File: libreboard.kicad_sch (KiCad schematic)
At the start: 41 parts, among them J100 Screw Terminal, J101 Screw Terminal, J11 USB_C_Receptacle_USB2.0, J51 12V Fan 1, J52 12V Fan 2, J53 12V Fan 3, J54 12V Fan 4, Q1 CSD18511Q5A, U4 LM5155DSSR

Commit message: starting to trace
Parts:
- added C31: 0.1uF, Capacitor_SMD:C_0402_1005Metric, symbol Device:C_Small
- added C51: 4.7 uF, Capacitor_SMD:C_0805_2012Metric, symbol Device:C_Small
- added C52, C53: 100 nF, Capacitor_SMD:C_0805_2012Metric, symbol Device:C_Small
- added C54, C55: 47 uF, Capacitor_SMD:C_0805_2012Metric, symbol Device:C_Small
- added L3: 5.6 uH, Inductor_SMD:L_Coilcraft_XAL6060-XXX, symbol Device:L
- added R21, R22, R23, R24, R29, R30: 10k, Resistor_SMD:R_0402_1005Metric, symbol Device:R_Small
- added R31: 22k, Resistor_SMD:R_0402_1005Metric, symbol Device:R_Small
- added R32: 33k, Resistor_SMD:R_0402_1005Metric, symbol Device:R_Small
- added R42: 30.9 kΩ, Resistor_SMD:R_0603_1608Metric, symbol Device:R_Small
- added R43, R44: 100 kΩ, Resistor_SMD:R_0603_1608Metric, symbol Device:R_Small
- added R45: 19.1 kΩ, Resistor_SMD:R_0603_1608Metric, symbol Device:R_Small
- added U10: EMC2305-x-AP, Package_DFN_QFN:Texas_RGV0016A_VQFN-16-1EP_4x4mm_P0.65mm_EP2.1x2.1mm_ThermalVias, symbol Driver_Motor:EMC2305-x-AP
- added U14: LMR51450FNDRRR, libreboard:CONV_LMR51450FNDRRR, symbol LMR51450FNDRRR:LMR51450FNDRRR
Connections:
- net +12V: now also J51.2 (12V), J52.2, J53.2, J54.2
- net +3.3v: now also C31.1, R21.1, R22.1, R23.1, R24.1, R29.2, R30.2, R31.2, R32.2, U10.3 (VDD)
- net +VDC: now also C51.1, C52.1, U14.10 (VIN), U14.11 (VIN__1), U14.12 (VIN__2), U14.9 (EN)
- net CM5_GPIO ( Ethernet, GPIO, SDCARD)/ID_SC: now also R30.1, U10.2 (SMCLK)
- net CM5_GPIO ( Ethernet, GPIO, SDCARD)/ID_SD: now also R29.1, U10.1 (SMDATA)
- net GND: now also J51.1 (GND), J52.1, J53.1, J54.1, C31.2, C51.2, C52.2, C54.2, C55.2, R42.2, R45.2, U10.17 (GND), U14.13 (PGND), U14.8 (AGND)
- net at J51.3 (TACH): now also R24.2, U10.6 (TACH1)
- net at J51.4 (PWM): now also U10.5 (PWM1)
- net at J52.3: now also R23.2, U10.8 (TACH2)
- net at J52.4: now also U10.7 (PWM2)
- net at J54.3: now also R21.2, U10.14 (TACH4)
- net at J54.4: now also U10.13 (PWM4)
- net at J53.3: now also R22.2, U10.10 (TACH3)
- net at J53.4: now also U10.9 (PWM3)
- new net: R44.2, R45.1, U14.7 (FB)
- new net: C53.2, L3.1, U14.1 (SW), U14.2 (SW__1), U14.3 (SW__2)
- new net: C53.1, U14.4 (BOOT)
- new net: R43.1, U14.5 (PG)
- new net: R42.1, U14.6 (RT)
- new net: R31.1, U10.11 (CLK)
- new net: R32.1, U10.4 (ADDR_SEL)
- new net +5V: C54.1, C55.1, L3.2, R43.2, R44.1
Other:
- sheet CM5_HighSpeed ports: added none; removed ID_SC, ID_SD
- note added: "https://webench.ti.com/appinfo/webench/scripts/SDP.cgi?ID=394641B4FF50B9DB"
- moved on the sheet: H1, H2, H3, H4, H5, H6, H7, H8, J100, J101, J51, J52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

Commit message: voltage regulator refactoring
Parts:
- removed C20, C21: 10uF, Capacitor_SMD:C_1210_3225Metric, symbol Device:C
- removed C22: 10nF, Capacitor_SMD:C_0603_1608Metric, symbol Device:C
- removed C23: 1uF, Capacitor_SMD:C_0603_1608Metric, symbol Device:C
- removed C24: 10pF, Capacitor_SMD:C_0201_0603Metric, symbol Device:C
- removed C25: 220nF, Capacitor_SMD:C_1812_4532Metric, symbol Device:C
- removed C26: 330pF, Capacitor_SMD:C_0402_1005Metric, symbol Device:C
- removed C27: 560pF, Capacitor_SMD:C_0805_2012Metric, symbol Device:C
- removed C28: 1uF, Capacitor_SMD:C_1206_3216Metric, symbol Device:C
- removed C29: 22uF, Capacitor_SMD:C_1210_3225Metric, symbol Device:C
- removed C30: 100pF, Capacitor_SMD:C_0805_2012Metric, symbol Device:C
- removed C51: 4.7 uF, Capacitor_SMD:C_0805_2012Metric, symbol Device:C_Small
- removed D4: 455mV 20A, Package_TO_SOT_THT:TO-220-2_Horizontal_TabDown, symbol Device:D_Schottky
- removed L2: 2.2uH, Inductor_SMD:L_Bourns_SRF1260, symbol Device:L_Iron_Coupled
- removed Q1: CSD18511Q5A, Package_SON:VSONP-8-1EP_5x6_P1.27mm, symbol emberone:CSD18511Q5A
- removed R11: 68.1kΩ, Resistor_SMD:R_0603_1608Metric, symbol Device:R
- removed R13: 100Ω, Resistor_SMD:R_0603_1608Metric, symbol Device:R
- removed R18: 51.1kΩ, Resistor_SMD:R_0603_1608Metric, symbol Device:R
- removed R19: 4.7kΩ, Resistor_SMD:R_0603_1608Metric, symbol Device:R
- removed R20: 18mΩ, Resistor_SMD:R_0612_1632Metric, symbol Device:R
- removed R42: 30.9 kΩ, Resistor_SMD:R_0603_1608Metric, symbol Device:R_Small
- removed R43, R44: 100 kΩ, Resistor_SMD:R_0603_1608Metric, symbol Device:R_Small
- removed R45: 19.1 kΩ, Resistor_SMD:R_0603_1608Metric, symbol Device:R_Small
- removed R6: 43.2kΩ, Resistor_SMD:R_0603_1608Metric, symbol Device:R
- removed R7: 6.49kΩ, Resistor_SMD:R_0603_1608Metric, symbol Device:R
- removed R8: 9.31kΩ, Resistor_SMD:R_0603_1608Metric, symbol Device:R
- removed U14: LMR51450FNDRRR, libreboard:CONV_LMR51450FNDRRR, symbol LMR51450FNDRRR:LMR51450FNDRRR
- removed U4: LM5155DSSR, libreboard:DSS0012B, symbol 2025-05-04_16-39-33:LM5155DSSR
- added C20: 39µF, Capacitor_SMD:CP_Elec_8x6.7, symbol Device:C_Polarized_Small
- added C21: 10µF, Capacitor_SMD:C_0402_1005Metric, symbol Device:C_Small
- added C22: 1µF, Capacitor_SMD:C_0603_1608Metric, symbol Device:C_Small
- added C23: 4.7µF, Capacitor_SMD:C_0603_1608Metric, symbol Device:C_Small
- added C24, C25, C65: 100nF, Capacitor_SMD:C_0603_1608Metric, symbol Device:C_Small
- added C26: 56µF, Capacitor_SMD:CP_Elec_5x5.9, symbol Device:C_Polarized_Small
- added C27, C28, C29: 33µF, Capacitor_SMD:C_0603_1608Metric, symbol Device:C_Small
- added C30, C64: 1µF, Capacitor_SMD:C_0402_1005Metric, symbol Device:C_Small
- added C51: 22µF, Capacitor_SMD:CP_Elec_6.3x5.9, symbol Device:C_Polarized_Small
- added C60: 3.9pF, Capacitor_SMD:C_0603_1608Metric, symbol Device:C_Small
- added C61: 470pF, Capacitor_SMD:C_0603_1608Metric, symbol Device:C_Small
- added C62: 560pF, Capacitor_SMD:C_0603_1608Metric, symbol Device:C_Small
- added C63: 1pF, Capacitor_SMD:C_0603_1608Metric, symbol Device:C_Small
- added C66, C67, C68: 47µF, Capacitor_SMD:C_0603_1608Metric, symbol Device:C_Small
- added C69: 270µF, Capacitor_SMD:CP_Elec_6.3x9.9, symbol Device:C_Polarized_Small
- added L2: 4.7µH, Inductor_SMD:L_Bourns_SRN8040TA, symbol Device:L
- added R11, R20: 105kΩ, Resistor_SMD:R_0603_1608Metric, symbol Device:R_Small
- added R13: 50kΩ, Resistor_SMD:R_0603_1608Metric, symbol Device:R_Small
- added R18, R6: 887kΩ, Resistor_SMD:R_0603_1608Metric, symbol Device:R_Small
- added R19, R7: 100kΩ, Resistor_SMD:R_0603_1608Metric, symbol Device:R_Small
- added R8: 48.7kΩ, Resistor_SMD:R_0603_1608Metric, symbol Device:R_Small
- added U14, U4: PTPS55289RYQR, libreboard:RYQ0021A-MFG, symbol TPS55289:PTPS55289RYQR
- C18, C9: value 100n -> 100nF; Dist. P/N (none) -> 478-11504-2-ND; Distributor (none) -> Digikey; Field4 Farnell -> (none); Field5 2611911 -> (none); Field6 RM EMK105 B7104KV-F -> (none); Field7 TAIYO YUDEN EUROPE GMBH -> (none); Field8 110091611 -> (none); Manf. P/N (none) -> 04026D104KAT4A; Manufacturer (none) -> Kyocera; Part Description 0.1uF 10% 16V Ceramic Capacitor X7R 0402 (1005 Metric) -> Capacitor, Ceramic, 0.1µF, ±10%, 6.3V, X5R, 0402 (1005m)
- C31: value 0.1uF -> 0.1µF; Dist. P/N (none) -> 478-11504-2-ND; Distributor (none) -> Digikey; Manf. P/N (none) -> 04026D104KAT4A; Manufacturer (none) -> Kyocera; Part Description (none) -> Capacitor, Ceramic, 0.1µF, ±10%, 6.3V, X5R, 0402 (1005m)
- C52: value 100 nF -> 10µF; footprint Capacitor_SMD:C_0805_2012Metric -> Capacitor_SMD:C_0402_1005Metric; Distributor (none) -> Digikey
- C53: value 100 nF -> 4.7µF; footprint Capacitor_SMD:C_0805_2012Metric -> Capacitor_SMD:C_0603_1608Metric; Distributor (none) -> Digikey
- C54: value 47 uF -> 1µF; footprint Capacitor_SMD:C_0805_2012Metric -> Capacitor_SMD:C_0603_1608Metric; Distributor (none) -> Digikey
- C55: value 47 uF -> 100nF; footprint Capacitor_SMD:C_0805_2012Metric -> Capacitor_SMD:C_0603_1608Metric; Distributor (none) -> Digikey
- H1, H2, H3, H4, H5, H6, H7, H8: Dist. P/N (none) -> nf; Distributor (none) -> nf; Field4 nf -> (none); Field5 nf -> (none); Field6 nf -> (none); Field7 nf -> (none)
- J100, J101: Dist. P/N (none) -> 36-7771-ND; Distributor (none) -> Digikey; Manf. P/N (none) -> 7771; Manufacturer (none) -> Keystone; Part Description (none) -> Screw Terminal, M3
- J11: footprint Connector_USB:USB_C_Receptacle_GCT_USB4105-xx-A_16P_TopMnt_Horizontal -> Connector_USB:USB_C_Receptacle_GCT_USB4105-GF-A_16P_TopMnt_Horizontal; Dist. P/N (none) -> 2073-USB4105-GF-ATR-ND; Distributor (none) -> Digikey; Field5 USBF31-0171 -> (none); Field6 USBF31-0171 -> (none); Field7 MTCONN -> (none); Manf. P/N (none) -> USB4105-GF-A; Manufacturer (none) -> GCT; Part Description USBC USB2 data and power connector -> Connector, USB-C, 2.0 data and power
- J51: Dist. P/N (none) -> WM4330-ND; Distributor (none) -> Digikey; Manf. P/N (none) -> 0470531000; Manufacturer (none) -> Molex; Part Description (none) -> Connector, Fan 1, 12V, 4 pin
- J52: Dist. P/N (none) -> WM4330-ND; Distributor (none) -> Digikey; Manf. P/N (none) -> 0470531000; Manufacturer (none) -> Molex; Part Description (none) -> Connector, Fan 2, 12V, 4 pin
- J53: Dist. P/N (none) -> WM4330-ND; Distributor (none) -> Digikey; Manf. P/N (none) -> 0470531000; Manufacturer (none) -> Molex; Part Description (none) -> Connector, Fan 3, 12V, 4 pin
- J54: Dist. P/N (none) -> WM4330-ND; Distributor (none) -> Digikey; Manf. P/N (none) -> 0470531000; Manufacturer (none) -> Molex; Part Description (none) -> Connector, Fan 4, 12V, 4 pin
- L3: value 5.6 uH -> 4.7µH; footprint Inductor_SMD:L_Coilcraft_XAL6060-XXX -> Inductor_SMD:L_Bourns_SRN8040TA; Dist. P/N (none) -> SRN8040-4R7YCT-ND; Distributor (none) -> Digikey; Manf. P/N (none) -> SRN8040-4R7Y; Manufacturer (none) -> Coilcraft; Part Description (none) -> FIXED IND 4.7UH 4.1A 24 MOHM SMD
- R21, R22, R23, R24, R29, R30: value 10k -> 10kΩ; Dist. P/N (none) -> 10-ERJ-U02F1002XTR-ND; Distributor (none) -> Digikey; Manf. P/N (none) -> ERJ-U02F1002X; Manufacturer (none) -> Panasonic; Part Description (none) -> Resistor, 10kΩ, ±1%, 0.1W, SMD 0402 (1005m)
- R31: value 22k -> 22kΩ; Dist. P/N (none) -> P22.0KLTR-ND; Distributor (none) -> Digikey; Manf. P/N (none) -> ERJ-2RKF2202X; Manufacturer (none) -> Panasonic; Part Description (none) -> Resistor, 22kΩ, ±1%, 0.1W, SMD 0402 (1005m)
- R32: value 33k -> 33kΩ; Dist. P/N (none) -> 10-ERJ-U02F3302XTR-ND; Distributor (none) -> Digikey; Manf. P/N (none) -> ERJ-U02F3302X; Manufacturer (none) -> Panasonic; Part Description (none) -> Resistor, 33kΩ, ±1%, 0.1W, SMD 0402 (1005m)
- R9: value 2.2K 1% -> 2.2kΩ; Dist. P/N (none) -> P2.20KLTR-ND; Distributor (none) -> Digikey; Field4 Farnell -> (none); Manf. P/N (none) -> ERJ-2RKF2201X; Manufacturer (none) -> Panasonic; Part Description Resistor 2.2K M1005 1% 63mW -> Resistor, 2.2kΩ, ±1%, 0.1W, SMD 0402 (1005m)
- U10: Dist. P/N (none) -> EMC2305-1-AP-TR-ND; Distributor (none) -> Digikey; Manf. P/N (none) -> EMC2305-1-AP-TR; Manufacturer (none) -> Microchip Technology; Part Description (none) -> Motor Driver, PWM, 16-QFN, 4x4
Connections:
- net +12V: now also C26.1, C27.1, C28.1, C29.1, C30.1, U4.11 (VOUT), U4.12 (ISP), U4.13 (ISN)
- net +5v: now also C64.1, C66.1, C67.1, C68.1, C69.1, U14.11 (VOUT), U14.12 (ISP), U14.13 (ISN)
- net +VDC: now also C54.1, C20.1, C21.1, C22.1, C51.1, R18.1, R6.1, U14.7 (VIN), U4.7 (VIN)
- net GND: now also C53.2, C20.2, C21.2, C22.2, C23.2, C26.2, C27.2, C28.2, C29.2, C30.2, C51.2, C60.2, C63.2, C64.2, C66.2, C67.2, C68.2, C69.2, R11.2, R13.2, R19.2, R20.2, R7.2, R8.2, U14.17 (AGND), U14.2 (MODE), U14.5 (DITH_SYNC), U14.9 (PGND), U4.17 (AGND), U4.2 (MODE), U4.5 (DITH_SYNC), U4.9 (PGND); no longer C55.2
- net at L3.1: now also C55.1, U14.8 (SW1); no longer C53.2
- net at C53.1: now also U14.18 (VCC), U14.21 (EXTVCC)
- removed net +5V: C54.1, C55.1, L3.2
- new net: C62.1, C63.1, U14.15 (COMP)
- new net: R6.2, R7.1, U4.1 (EN_UVLO)
- new net: C25.1, L2.2, U4.10 (SW2)
- new net: C60.1, C61.1, U4.15 (COMP)
- new net: C23.1, U4.18 (VCC), U4.21 (EXTVCC)
- new net: C25.2, U4.19 (BOOT2)
- new net: C24.2, U4.20 (BOOT1)
- new net: R8.1, U4.6 (FSW)
- new net: C24.1, L2.1, U4.8 (SW1)
- new net: C62.2, R20.1
- new net: C65.1, L3.2, U14.10 (SW2)
- new net: C61.2, R11.1
- new net: R13.1, U14.6 (FSW)
- new net: C55.2, U14.20 (BOOT1)
- new net: R18.2, R19.1, U14.1 (EN_UVLO)
- new net: C65.2, U14.19 (BOOT2)
- no-connect marks 2 -> 6
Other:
- note added: "https://webench.ti.com/appinfo/webench/scripts/SDP.cgi?ID=1FB30C76529277AD"
- note added: "https://webench.ti.com/appinfo/webench/scripts/SDP.cgi?ID=DFB867964FE642FB"
- note removed: "https://webench.ti.com/appinfo/webench/scripts/SDP.cgi?ID=394641B4FF50B9DB"

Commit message: place all components
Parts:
- C22, C23, C24, C25, C27, C28, C29, C53, C54, C55, C60, C61, C62, C63, C65, C66, C67, C68: footprint Capacitor_SMD:C_0603_1608Metric -> Capacitor_SMD:C_0402_1005Metric
- J100, J101: footprint libreboard:7770-screw-terminal -> libreboard:KEYSTONE_7790; Dist. P/N 36-7771-ND -> 36-7790-ND; Manf. P/N 7771 -> 7790
- J54: now not fitted
- R11, R13, R18, R19, R20, R6, R7, R8: footprint Resistor_SMD:R_0603_1608Metric -> Resistor_SMD:R_0402_1005Metric

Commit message: updates BOM, sychronizes PCB from schematic, & includes error report.
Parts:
- C20: Dist. P/N (none) -> 399-A770KE396M1HLAS042TR-ND; Distributor (none) -> Digikey; Manf. P/N (none) -> A770KE396M1HLAS042; Manufacturer (none) -> Kemet; Part Description (none) -> Capacitor, Aluminum, 39µF, ±20%, 50V, 42mΩ ESR
- C21, C52: Dist. P/N (none) -> 478-KGM05CR50J106MHTR-ND; Manf. P/N (none) -> 04026D106MAT2A; Manufacturer (none) -> Kyocera; Part Description (none) -> Capacitor, Ceramic, 10µF, ±20%, 6.3V, X5R, 0402 (1005m)
- C22, C30, C54, C64: Dist. P/N (none) -> 478-KGM05AR50J105KHTR-ND; Manf. P/N (none) -> 04026D105KAT2A; Manufacturer (none) -> Kyocera; Part Description (none) -> Capacitor, Ceramic, 1µF, ±10%, 6.3V, X5R, 0402 (1005m)
- C23, C53: footprint Capacitor_SMD:C_0402_1005Metric -> Capacitor_SMD:C_1206_3216Metric; Dist. P/N (none) -> 478-KGM31AR71H475KUTR-ND; Manf. P/N (none) -> 12065C475KAT2A; Manufacturer (none) -> Kyocera; Part Description (none) -> Capacitor, Ceramic, 4.7µF, ±10%, 50V, X7R, 1206 (3216m)
- C24, C25, C55, C65: Dist. P/N (none) -> 478-11504-2-ND; Manf. P/N (none) -> 04026D104KAT4A; Manufacturer (none) -> Kyocera; Part Description (none) -> Capacitor, Ceramic, 0.1µF, ±10%, 6.3V, X5R, 0402 (1005m)
- C26: Dist. P/N (none) -> P122099TR-ND; Distributor (none) -> Digikey; Manf. P/N (none) -> 20SVF56M; Manufacturer (none) -> Panasonic; Part Description (none) -> Capacitor, Aluminum, 56µF, ±20%, 20V, 30mΩ ESR
- C51: Dist. P/N (none) -> 399-A768EB226M1HLAE048TR-ND; Distributor (none) -> Digikey; Manf. P/N (none) -> A768EB226M1HLAE048; Manufacturer (none) -> Kemet; Part Description (none) -> Capacitor, Aluminum, 22µF, ±20%, 50V, 48mΩ ESR
- C60: Dist. P/N (none) -> 478-KGM05ACG1H3R9BHTR-ND; Manf. P/N (none) -> KGM05ACG1H3R9BH; Manufacturer (none) -> Kyocera; Part Description (none) -> Capacitor, Ceramic, 3.9pF, ±2.5%, 50V, C0G/NP0, 0402 (1005m)
- C61: Dist. P/N (none) -> 478-KGM05AR71H471KHTR-ND; Manf. P/N (none) -> KGM05AR71H471KH; Manufacturer (none) -> Kyocera; Part Description (none) -> Capacitor, Ceramic, 470pF, ±10%, 50V, X7R, 0402 (1005m)
- C62: Dist. P/N (none) -> 478-1098-2-ND; Manf. P/N (none) -> 04025C561KAT2A; Manufacturer (none) -> Kyocera; Part Description (none) -> Capacitor, Ceramic, 560pF, ±10%, 50V, X7R, 0402 (1005m)
- C63: Dist. P/N (none) -> 478-KGQ05FCG1H1R0BHTR-ND; Manf. P/N (none) -> 04025U1R0BAT2A; Manufacturer (none) -> Kyocera; Part Description (none) -> Capacitor, Ceramic, 1pF, ±10%, 50V, C0G/NP0, 0402 (1005m)
- C66, C67, C68: Dist. P/N (none) -> 732-7429-2-ND; Manf. P/N (none) -> 885012005011; Manufacturer (none) -> Würth Elektronik; Part Description (none) -> Capacitor, Ceramic, 47pF, ±5%, 10V, C0G/NP0, 0402 (1005m)
- C69: Dist. P/N (none) -> P16432TR-ND; Distributor (none) -> Digikey; Manf. P/N (none) -> 10SVP270M; Manufacturer (none) -> Panasonic; Part Description (none) -> Capacitor, Aluminum, 270µF, ±20%, 10V, 25mΩ ESR
- R11, R20: Dist. P/N (none) -> P105KLTR-ND; Manf. P/N (none) -> ERJ-2RKF1053X; Manufacturer (none) -> Panasonic; Part Description 50 mW -> Resistor, 105kΩ, ±1%, 0.1W, SMD 0402 (1005m)
- R13: Dist. P/N (none) -> 541-CRCW040250K0FKEDTR-ND; Manf. P/N (none) -> CRCW040250K0FKED; Manufacturer (none) -> Vishay Dale; Part Description (none) -> Resistor, 50kΩ, ±1%, 0.1W, SMD 0402 (1005m)
- R18, R6: Dist. P/N (none) -> P887KLTR-ND; Manf. P/N (none) -> ERJ-2RKF8873X; Manufacturer (none) -> Panasonic; Part Description (none) -> Resistor, 887kΩ, ±1%, 0.1W, SMD 0402 (1005m)
- R19, R7: Dist. P/N (none) -> 10-ERJ-U02F1003XTR-ND; Manf. P/N (none) -> ERJ-U02F1003X; Manufacturer (none) -> Panasonic; Part Description (none) -> Resistor, 100kΩ, ±1%, 0.1W, SMD 0402 (1005m)
- R8: Dist. P/N (none) -> P48.7KLTR-ND; Manf. P/N (none) -> ERJ-2RKF4872X; Manufacturer (none) -> Panasonic; Part Description (none) -> Resistor, 48.7kΩ, ±1%, 0.1W, SMD 0402 (1005m)
- U14, U4: Dist. P/N (none) -> 296-TPS55289RYQRTR-ND; Distributor (none) -> Digikey; Manf. P/N (none) -> TPS55289RYQR; Manufacturer (none) -> Texas Instruments; Part Description (none) -> IC, Buck Boost, 0.8v, 1-output, 8A

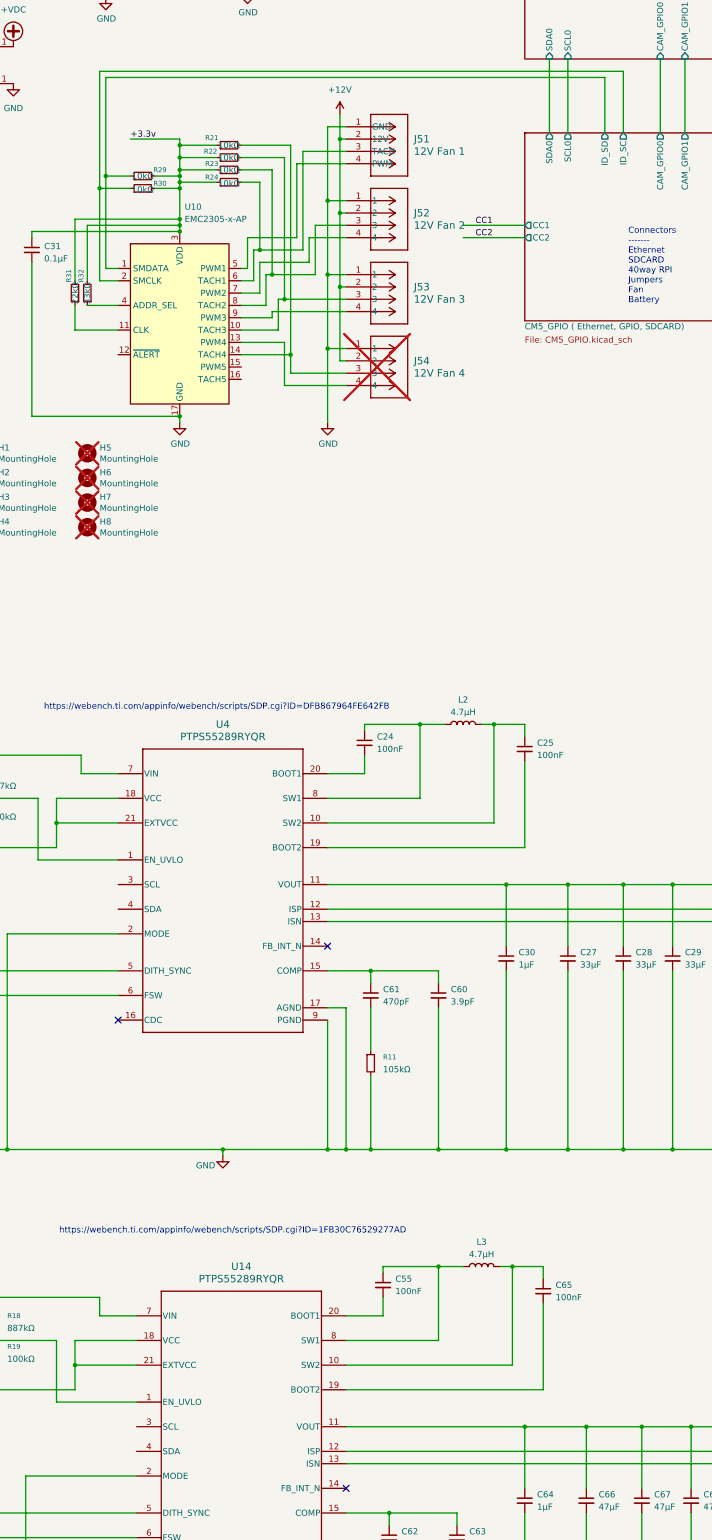
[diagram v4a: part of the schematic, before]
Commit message: change C27-C29 to 1206, reroute i2c
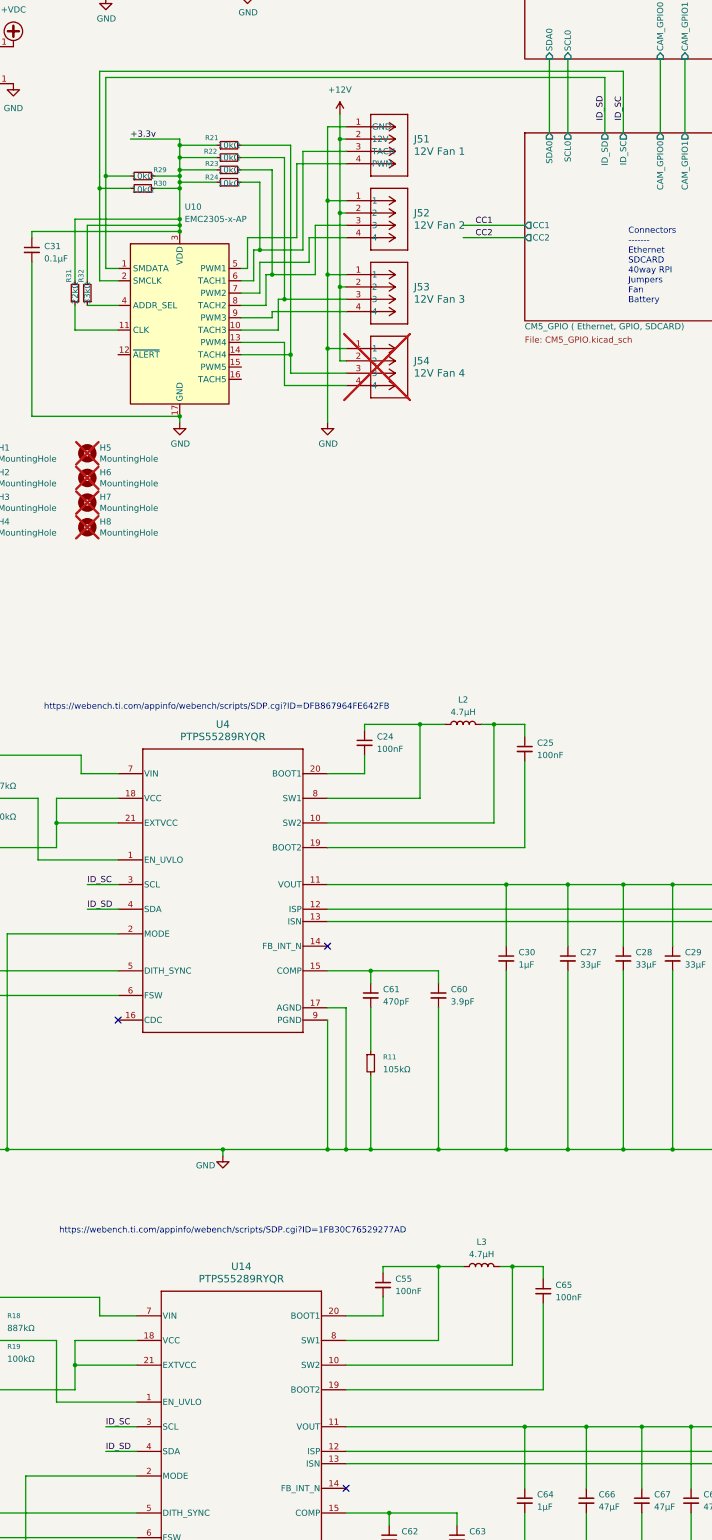
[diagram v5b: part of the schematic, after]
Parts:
- C27, C28, C29: footprint Capacitor_SMD:C_0402_1005Metric -> Capacitor_SMD:C_1206_3216Metric
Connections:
- net CM5_GPIO ( Ethernet, GPIO, SDCARD)/ID_SC is gone; now on net ID_SC: R30.1, U10.2 (SMCLK)
- net CM5_GPIO ( Ethernet, GPIO, SDCARD)/ID_SD is gone; now on net ID_SD: R29.1, U10.1 (SMDATA)
- net ID_SC: now reaches U4.3 (SCL)
- net ID_SC: now also U14.3 (SCL)
- net ID_SD: now reaches U4.4 (SDA)
- net ID_SD: now also U14.4 (SDA)
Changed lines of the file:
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@@
 	(wire
 		(pts
+			(xy 39.37 266.7) (xy 45.72 266.7)
+		)
+		(stroke
+			(width 0)
+			(type default)
+		)
+	)
+	(wire
+		(pts
 			(xy 101.6 433.07) (xy 115.57 433.07)
 		)
@@
 	(wire
 		(pts
+			(xy 43.18 383.54) (xy 49.53 383.54)
+		)
+		(stroke
+			(width 0)
+			(type default)
+		)
+	)
+	(wire
+		(pts
 			(xy 45.72 261.62) (xy 29.21 261.62)
 		)
@@
 	(wire
 		(pts
+			(xy 39.37 271.78) (xy 45.72 271.78)
+		)
+		(stroke
+			(width 0)
+			(type default)
+		)
+	)
+	(wire
+		(pts
 			(xy 16.51 321.31) (xy 22.86 321.31)
 		)
@@
 	(wire
 		(pts
+			(xy 43.18 378.46) (xy 49.53 378.46)
+		)
+		(stroke
+			(width 0)
+			(type default)
+		)
+	)
+	(wire
+		(pts
 			(xy 58.42 114.3) (xy 66.04 114.3)
 		)
@@
 		)
 	)
+	(label "ID_SC"
+		(at 39.37 266.7 0)
+		(effects
+			(font
+				(size 1.27 1.27)
+			)
+			(justify left bottom)
+		)
+	)
 	(label "CC2"
 		(at 119.38 133.35 0)
@@
 		)
 	)
+	(label "ID_SC"
+		(at 149.86 109.22 90)
+		(effects
+			(font
+				(size 1.27 1.27)
+			)
+			(justify left bottom)
+		)
+	)
+	(label "ID_SC"
+		(at 43.18 378.46 0)
+		(effects
+			(font
+				(size 1.27 1.27)
+			)
+			(justify left bottom)
+		)
+	)
+	(label "ID_SD"
+		(at 39.37 271.78 0)
+		(effects
+			(font
+				(size 1.27 1.27)
+			)
+			(justify left bottom)
+		)
+	)
 	(label "USB2_P"
 		(at 74.93 62.23 180)
@@
 		)
 	)
+	(label "ID_SD"
+		(at 146.05 109.22 90)
+		(effects
+			(font
+				(size 1.27 1.27)
+			)
+			(justify left bottom)
+		)
+	)
 	(label "USB2_N"
 		(at 74.93 57.15 180)
@@
 		)
 	)
+	(label "ID_SD"
+		(at 43.18 383.54 0)
+		(effects
+			(font
+				(size 1.27 1.27)
+			)
+			(justify left bottom)
+		)
+	)
 	(symbol
 		(lib_id "Mechanical:MountingHole")
@@
 			)
 		)
-		(property "Footprint" "Capacitor_SMD:C_0402_1005Metric"
+		(property "Footprint" "Capacitor_SMD:C_1206_3216Metric"
 			(at 149.86 281.94 0)
 			(effects
@@
 			)
 		)
-		(property "Footprint" "Capacitor_SMD:C_0402_1005Metric"
+		(property "Footprint" "Capacitor_SMD:C_1206_3216Metric"
 			(at 160.02 281.94 0)
 			(effects
@@
 			)
 		)
-		(property "Footprint" "Capacitor_SMD:C_0402_1005Metric"
+		(property "Footprint" "Capacitor_SMD:C_1206_3216Metric"
 			(at 138.43 281.94 0)
 			(effects

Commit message: C27-C29 update
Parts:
- C27, C28, C29: Dist. P/N (none) -> 445-8046-1-ND - Cut Tape; Manf. P/N (none) -> C3216X5R1E336M160AC; Manufacturer (none) -> TDK Corporation; Part Description (none) -> 33 µF ±20% 25V Ceramic Capacitor X5R 1206 (3216 Metric)
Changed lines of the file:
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@@
 			)
 		)
-		(property "Datasheet" ""
+		(property "Datasheet" "https://product.tdk.com/system/files/dam/doc/product/capacitor/ceramic/mlcc/catalog/mlcc_commercial_general_en.pdf"
 			(at 149.86 281.94 0)
 			(effects
@@
 			)
 		)
-		(property "Dist. P/N" ""
+		(property "Dist. P/N" "445-8046-1-ND - Cut Tape"
 			(at 149.86 281.94 0)
 			(effects
@@
 			)
 		)
-		(property "Manf. P/N" ""
+		(property "Manf. P/N" "C3216X5R1E336M160AC"
 			(at 149.86 281.94 0)
 			(effects
@@
 			)
 		)
-		(property "Manufacturer" ""
+		(property "Manufacturer" "TDK Corporation"
 			(at 149.86 281.94 0)
 			(effects
@@
 			)
 		)
-		(property "Part Description" ""
+		(property "Part Description" "33 µF ±20% 25V Ceramic Capacitor X5R 1206 (3216 Metric)"
 			(at 149.86 281.94 0)
 			(effects
@@
 			)
 		)
-		(property "Datasheet" ""
+		(property "Datasheet" "https://product.tdk.com/system/files/dam/doc/product/capacitor/ceramic/mlcc/catalog/mlcc_commercial_general_en.pdf"
 			(at 160.02 281.94 0)
 			(effects
@@
 			)
 		)
-		(property "Dist. P/N" ""
+		(property "Dist. P/N" "445-8046-1-ND - Cut Tape"
 			(at 160.02 281.94 0)
 			(effects
@@
 			)
 		)
-		(property "Manf. P/N" ""
+		(property "Manf. P/N" "C3216X5R1E336M160AC"
 			(at 160.02 281.94 0)
 			(effects
@@
 			)
 		)
-		(property "Manufacturer" ""
+		(property "Manufacturer" "TDK Corporation"
 			(at 160.02 281.94 0)
 			(effects
@@
 			)
 		)
-		(property "Part Description" ""
+		(property "Part Description" "33 µF ±20% 25V Ceramic Capacitor X5R 1206 (3216 Metric)"
 			(at 160.02 281.94 0)
 			(effects
@@
 			)
 		)
-		(property "Datasheet" ""
+		(property "Datasheet" "https://product.tdk.com/system/files/dam/doc/product/capacitor/ceramic/mlcc/catalog/mlcc_commercial_general_en.pdf"
 			(at 138.43 281.94 0)
 			(effects
@@
 			)
 		)
-		(property "Dist. P/N" ""
+		(property "Dist. P/N" "445-8046-1-ND - Cut Tape"
 			(at 138.43 281.94 0)
 			(effects
@@
 			)
 		)
-		(property "Manf. P/N" ""
+		(property "Manf. P/N" "C3216X5R1E336M160AC"
 			(at 138.43 281.94 0)
 			(effects
@@
 			)
 		)
-		(property "Manufacturer" ""
+		(property "Manufacturer" "TDK Corporation"
 			(at 138.43 281.94 0)
 			(effects
@@
 			)
 		)
-		(property "Part Description" ""
+		(property "Part Description" "33 µF ±20% 25V Ceramic Capacitor X5R 1206 (3216 Metric)"
 			(at 138.43 281.94 0)
 			(effects
